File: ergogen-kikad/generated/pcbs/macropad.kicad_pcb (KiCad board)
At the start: 2 copper layers, 75 x 82 mm, 9 parts

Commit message: Update PCB generation, labeling, and routing
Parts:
- moved S8 287.9 mm to (235.5, 173.5)
- moved S4 278.2 mm to (235.5, 123.5)
- moved S6 276.9 mm to (199.5, 173.5)
- moved S2 264.4 mm to (199.5, 123.5)
- moved MCU1 251.1 mm to (236.5, 148.5)
- moved S7 238.4 mm to (217.5, 173.5)
- moved S3 234.6 mm to (217.5, 123.5)
- moved S5 226.4 mm to (181.5, 173.5)
- moved S1 219.5 mm to (181.5, 123.5)
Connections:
- MCU1 pad 1: K0 -> (no net)
- MCU1 pad 10: (no net) -> D9
- MCU1 pad 11: (no net) -> D10
- MCU1 pad 2: K1 -> (no net)
- MCU1 pad 3: K2 -> (no net)
- MCU1 pad 4: K3 -> D3
- MCU1 pad 5: K4 -> D4
- MCU1 pad 6: K5 -> D5
- MCU1 pad 7: K6 -> D6
- MCU1 pad 8: K7 -> D7
- MCU1 pad 9: (no net) -> D8
- S1 pad 2: K4 -> D6
- S2 pad 2: K0 -> D5
- S3 pad 2: K5 -> D4
- S4 pad 2: K1 -> D3
- S5 pad 1: GND -> D7
- S5 pad 2: K6 -> GND
- S6 pad 1: GND -> D8
- S6 pad 2: K2 -> GND
- S7 pad 1: GND -> D9
- S7 pad 2: K7 -> GND
- S8 pad 1: GND -> D10
- S8 pad 2: K3 -> GND
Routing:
- net K0: track 112.0 -> 0.00 mm
- net K4: track 109.9 -> 0.00 mm
- net K1: track 88.5 -> 0.00 mm
- net K5: track 85.3 -> 0.00 mm
- net D6: track 0.00 -> 66.7 mm
- net K2: track 64.9 -> 0.00 mm
- net K6: track 60.8 -> 0.00 mm
- net D7: track 0.00 -> 59.6 mm
- net D5: track 0.00 -> 52.3 mm
- net D8: track 0.00 -> 45.2 mm
- net K3: track 44.9 -> 0.00 mm
- net D4: track 0.00 -> 37.9 mm
- net D9: track 0.00 -> 30.8 mm
- net D3: track 0.00 -> 23.5 mm
- net K7: track 17.7 -> 0.00 mm
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
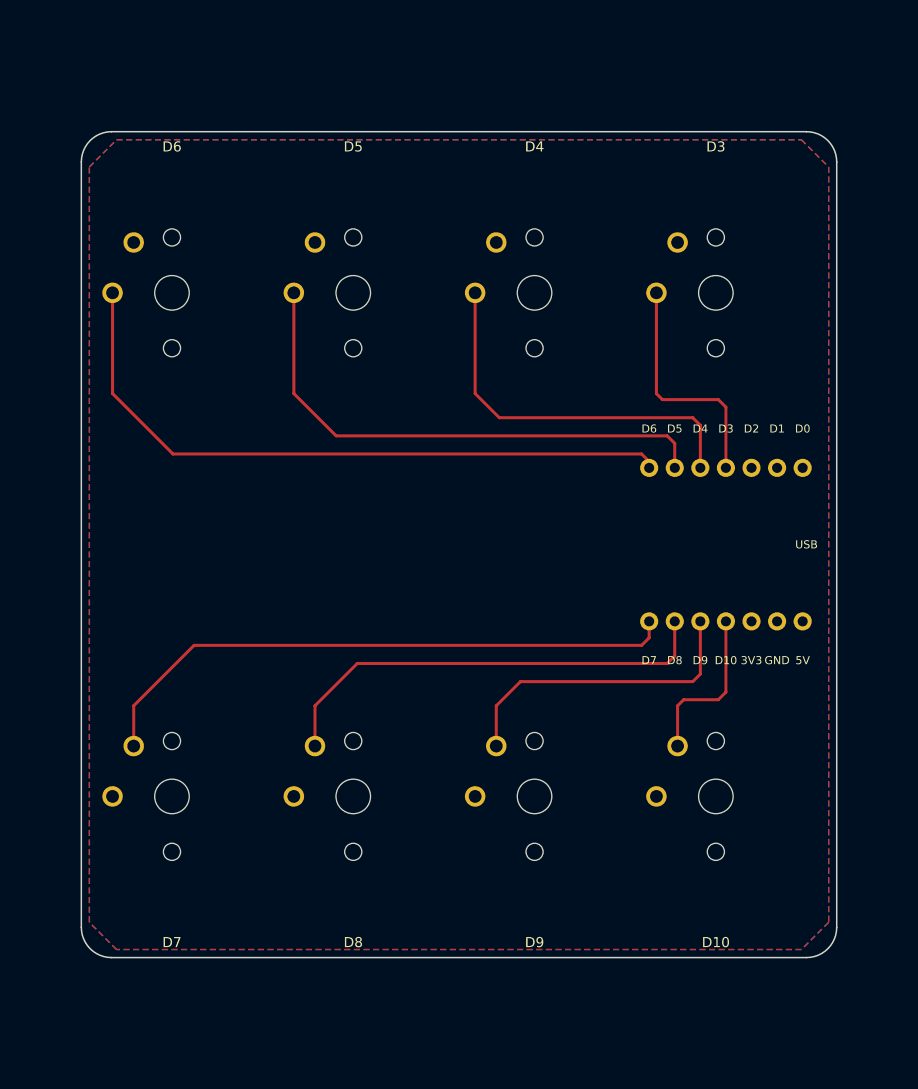
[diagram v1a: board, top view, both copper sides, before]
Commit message: Add circuit-free base plate and MagSafe alignment marker
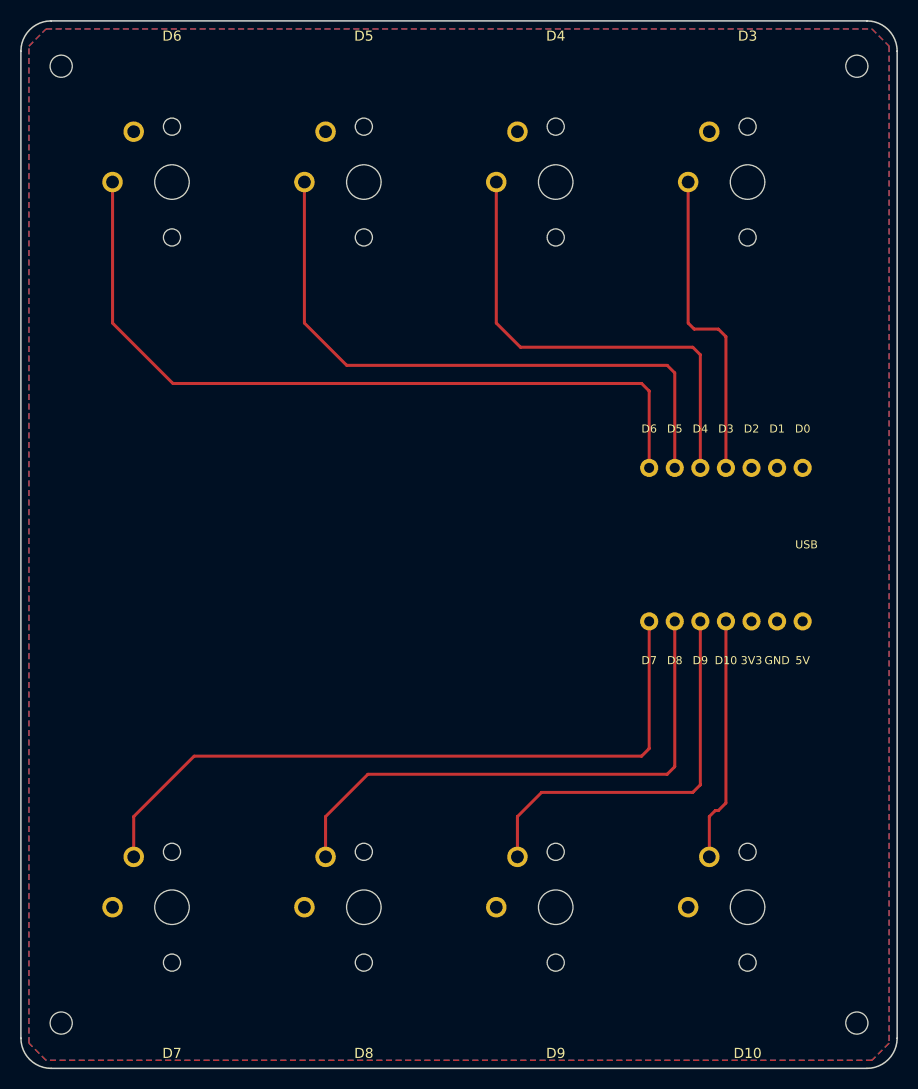
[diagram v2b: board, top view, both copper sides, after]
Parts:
- added H1: M2 mount, M2_Mount, F.Cu at (170.5, 101.0)
- added H2: M2 mount, M2_Mount, F.Cu at (249.5, 101.0)
- added H3: M2 mount, M2_Mount, F.Cu at (170.5, 196.0)
- added H4: M2 mount, M2_Mount, F.Cu at (249.5, 196.0)
- moved S4 11.4 mm to (238.7, 112.5)
- moved S8 11.4 mm to (238.7, 184.5)
- moved S3 11.2 mm to (219.6, 112.5)
- moved S7 11.2 mm to (219.6, 184.5)
- moved S2 11.1 mm to (200.6, 112.5)
- moved S6 11.1 mm to (200.6, 184.5)
- moved S1 11.0 mm to (181.5, 112.5)
- moved S5 11.0 mm to (181.5, 184.5)
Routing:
- net D7: track 59.6 -> 70.6 mm
- net D6: track 66.7 -> 77.7 mm
- net D8: track 45.2 -> 55.2 mm
- net D5: track 52.3 -> 62.3 mm
- net D9: track 30.8 -> 39.7 mm
- net D4: track 37.9 -> 46.8 mm
- net D10: track 16.4 -> 24.2 mm
- net D3: track 23.5 -> 31.3 mm
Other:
- board size 75 x 82 mm -> 87 x 104 mm

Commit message: Compact PCB and add Mill-Max socket clearances
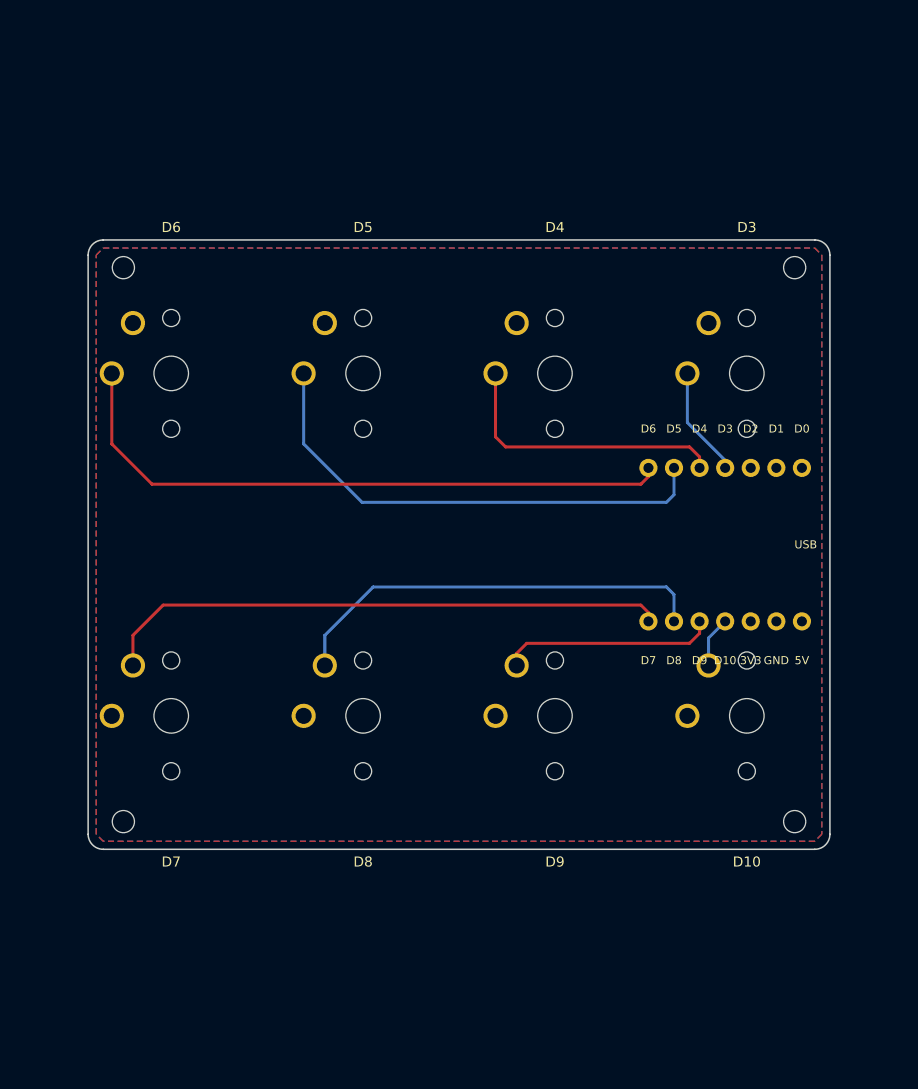
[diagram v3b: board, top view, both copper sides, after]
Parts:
- moved H1 20.9 mm to (176.7, 121.0)
- moved H2 20.9 mm to (243.3, 121.0)
- moved H3 20.9 mm to (176.7, 176.0)
- moved H4 20.9 mm to (243.3, 176.0)
- moved S2 19.0 mm to (200.5, 131.5)
- moved S4 19.0 mm to (238.6, 131.5)
- moved S6 19.0 mm to (200.5, 165.5)
- moved S8 19.0 mm to (238.6, 165.5)
- moved S1 19.0 mm to (181.4, 131.5)
- moved S3 19.0 mm to (219.5, 131.5)
- moved S5 19.0 mm to (181.4, 165.5)
- moved S7 19.0 mm to (219.5, 165.5)
- moved MCU1 0.07 mm to (236.4, 148.5)
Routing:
- net D3: track 31.3 -> 10.9 mm
- net D10: track 24.2 -> 5.06 mm
- net D4: track 46.8 -> 28.5 mm
- net D9: track 39.7 -> 21.4 mm
- net D6: track 77.7 -> 63.1 mm
- net D7: track 70.6 -> 56.6 mm
- net D5: track 62.3 -> 49.2 mm
- net D8: track 55.2 -> 42.6 mm
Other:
- board size 87 x 104 mm -> 73.6 x 60.5 mm
